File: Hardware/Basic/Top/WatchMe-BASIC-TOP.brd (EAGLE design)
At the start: 38 x 38 mm, 65 parts, among them SW1 SWITCH.MOM, SW2 SWITCH.MOM, U2 NRF52832_MODULE_MDBT42, U4 PCF8523, U5 FT231XS

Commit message: continuin top board work
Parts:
- removed C10, C11: 300p, LinnesLab-Passives:C0603
- removed R15: 100k, LinnesLab-Passives:R0603
- moved R19 49.2 mm to (12.4, 10.7), turned to 90 degrees
- moved R9 48.6 mm to (7.85, 15.5), turned to 0 degrees
- moved JP2 47.7 mm to (2.29, 7.72)
- moved LED5 47.6 mm to (13.9, 10.5), turned to 90 degrees
- moved C2 47.6 mm to (9.70, 2.11), turned to 0 degrees
- moved R20 46.7 mm to (3.20, 4.42)
- moved U5 46.4 mm to (7.24, 8.84)
- moved LED6 46.2 mm to (7.75, 3.58)
- moved C22 46.1 mm to (15.3, 9.09)
- moved R17 45.5 mm to (12.1, 7.34)
- moved R18 45.5 mm to (12.1, 4.19)
- moved C24 44.9 mm to (13.6, 7.39)
- moved D1 44.9 mm to (3.20, 24.4), turned to 180 degrees
- moved C23 44.9 mm to (13.6, 4.19)
- moved R8 44.7 mm to (11.5, 13.2), turned to 0 degrees
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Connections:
- net 3.3V: no longer R15.2
- net GND: no longer C10.2, C11.2, R15.1, SW1.B2, SW2.B2
- net P0.09/NFC1: no longer C11.1
- net P0.10/NFC2: no longer C10.1
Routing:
- net GND: track 0.00 -> 49.8 mm, vias 0 -> 20
- net D15/SW2: track 0.00 -> 35.7 mm
- net VLIPO: track 0.00 -> 13.8 mm
- net N$6: track 0.00 -> 10.9 mm
- net N$4: track 0.00 -> 10.8 mm
- net VIN: track 0.00 -> 10.4 mm
- net N$15: track 0.00 -> 10.4 mm
- net N$2: track 0.00 -> 10.1 mm
- net RESET: track 0.00 -> 9.97 mm
- net N$13: track 0.00 -> 9.50 mm
- net RXD.FT: track 0.00 -> 8.97 mm
- net SCL: track 0.00 -> 8.36 mm
- net V_USB: track 0.00 -> 7.84 mm
- net SDA: track 0.00 -> 7.11 mm
- net 3.3V: track 0.00 -> 4.59 mm, vias 0 -> 1
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- added copper zone on layer 1, net 9V
- added copper zone on layer 16, net GND

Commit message: updated top board, still pretty chaotic
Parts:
- moved SW3 27.6 mm to (14.1, 30.9), turned to 180 degrees
- moved LED4 26.1 mm to (14.5, 28.7), turned to 0 degrees
- moved LED3 26.0 mm to (14.4, 24.6), turned to 0 degrees
- moved R4 25.9 mm to (14.5, 27.4), turned to 0 degrees
- moved R3 25.9 mm to (14.5, 25.9), turned to 0 degrees
- moved C21 5.10 mm to (16.7, 11.3), turned to 180 degrees
- moved XTAL3 1.67 mm to (17.8, 22.8)
- moved SW2 1.15 mm to (22.3, 4.22)
- moved R14 1.04 mm to (18.1, 13.7)
- moved R13 0.97 mm to (16.5, 13.7)
- moved XTAL2 0.62 mm to (20.3, 22.4)
- moved L2 0.41 mm to (24.1, 25.1)
- moved J2 0.40 mm to (2.34, 16.3)
- moved C12 0.33 mm to (23.4, 22.6)
- moved CHRG2 0.23 mm to (8.92, 4.01)
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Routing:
- net RXD.NRF: track 0.00 -> 41.7 mm, vias 0 -> 2
- net MOSI: track 0.00 -> 40.1 mm, vias 0 -> 2
- net USB+: track 1.47 -> 40.1 mm, vias 0 -> 2
- net SWO: track 0.00 -> 36.8 mm, vias 0 -> 1
- net SCK: track 0.00 -> 35.4 mm, vias 0 -> 2
- net SWCLK: track 0.00 -> 34.6 mm, vias 0 -> 1
- net RESET: track 9.97 -> 44.2 mm, vias 0 -> 2
- net TXD.NRF: track 0.00 -> 32.8 mm, vias 0 -> 2
- net SWDIO: track 0.00 -> 32.4 mm, vias 0 -> 1
- net GND: track 49.8 -> 80.1 mm, vias 20 -> 23
- net D11/SW1: track 0.00 -> 29.9 mm, vias 0 -> 2
- net D27/CHRG.STATUS: track 3.97 -> 32.0 mm, vias 0 -> 1
- net USB-: track 1.52 -> 28.5 mm, vias 0 -> 1
- net D16/CS.OLED: track 0.00 -> 26.6 mm, vias 0 -> 2
- net D7/SD.CS: track 0.00 -> 26.1 mm, vias 0 -> 1
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
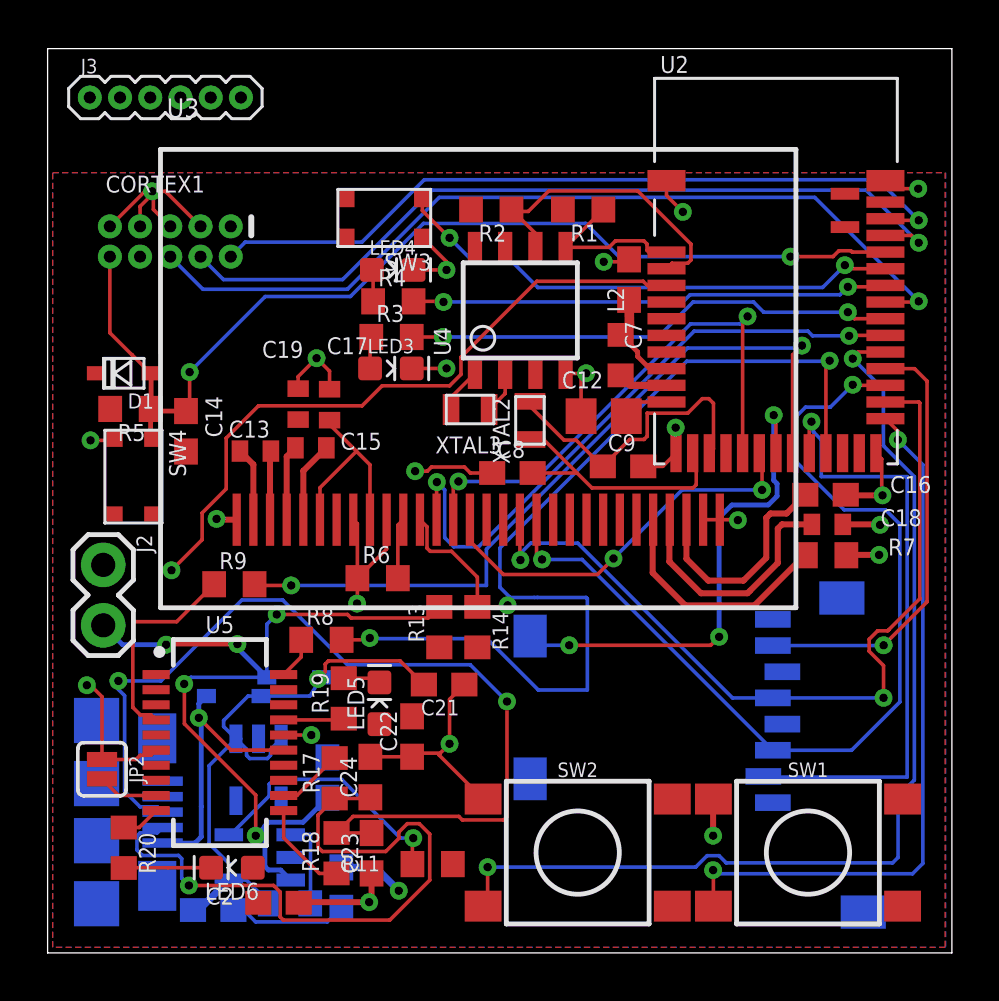
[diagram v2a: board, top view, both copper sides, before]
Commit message: top board routing complete
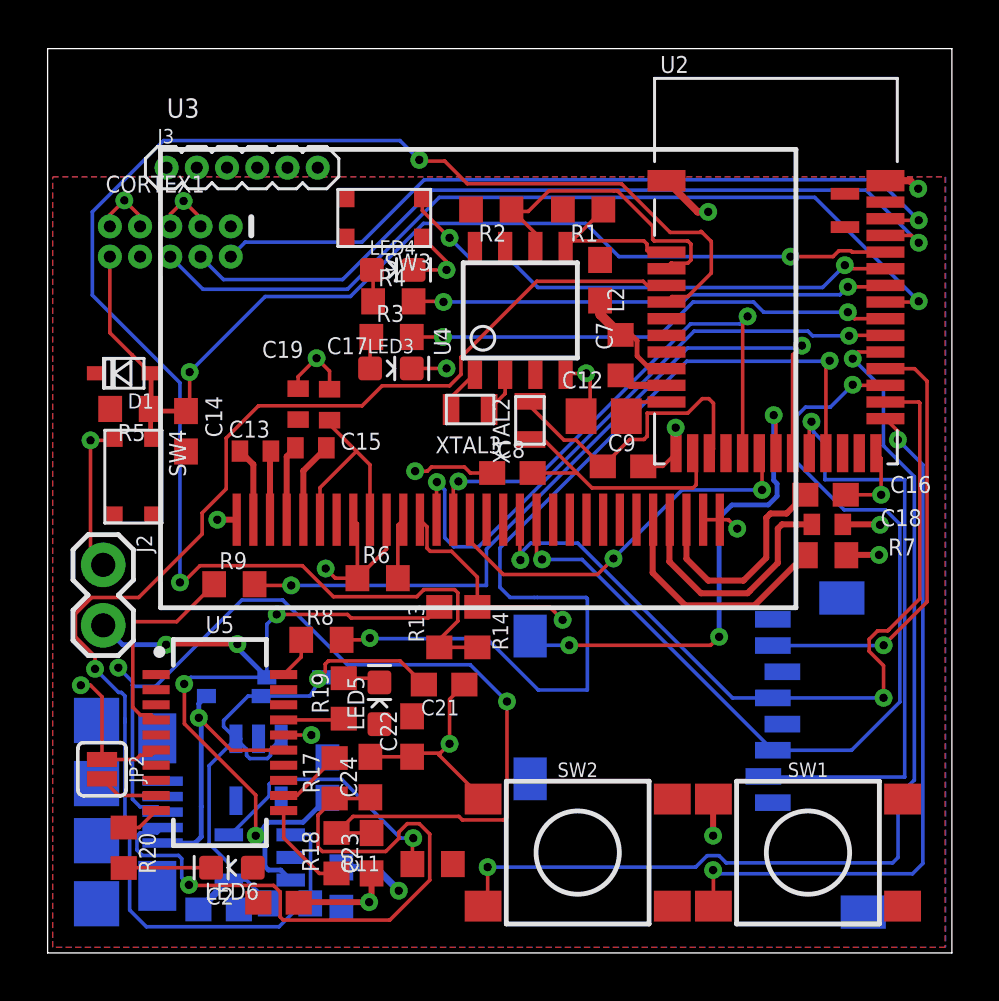
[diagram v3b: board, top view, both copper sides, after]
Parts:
- moved J3 4.37 mm to (5.00, 33.0)
- moved C7 1.22 mm to (23.2, 28.3)
- moved C5 0.23 mm to (7.19, 1.83)
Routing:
- net A4/BATT: track 0.00 -> 66.8 mm, vias 0 -> 2
- net D27/CHRG.STATUS: track 32.0 -> 58.5 mm
- net GND: track 80.1 -> 81.1 mm
- net SCL: track 13.2 -> 14.0 mm

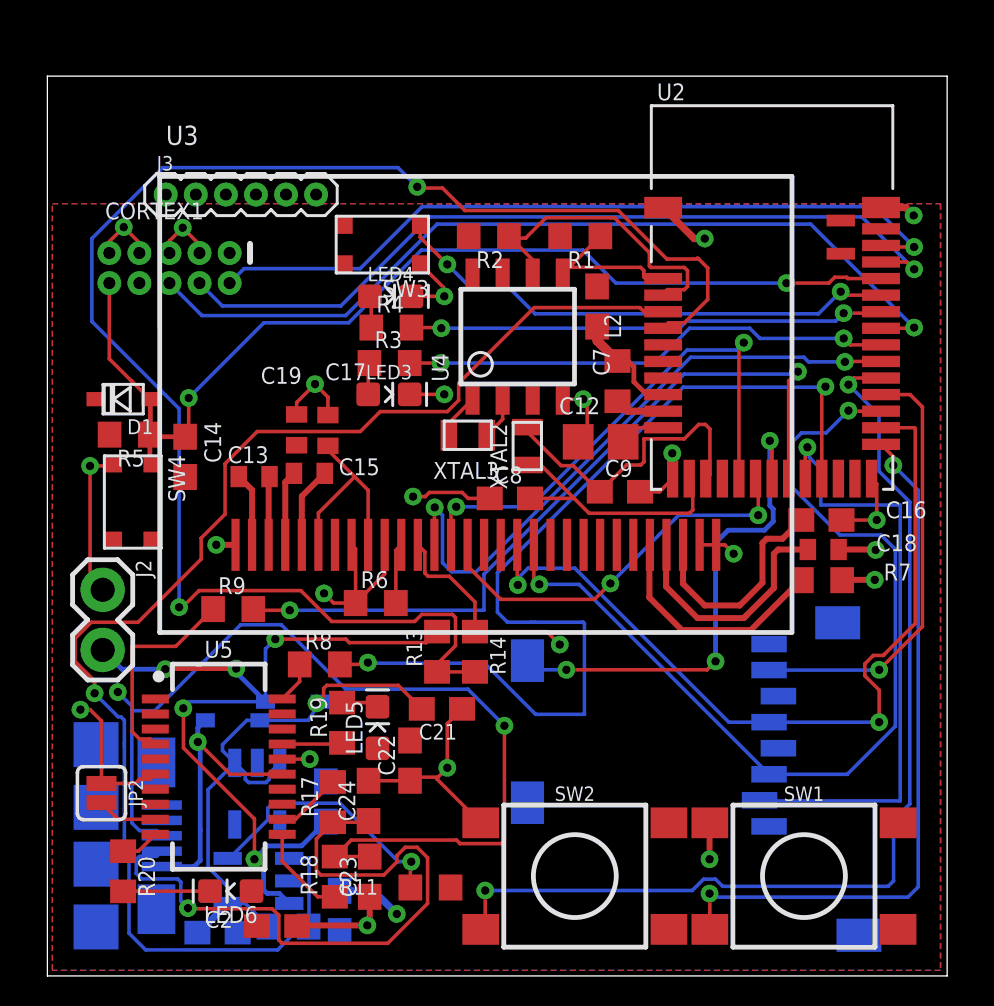
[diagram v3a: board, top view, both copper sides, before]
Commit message: Added LSM6DS3 sensor
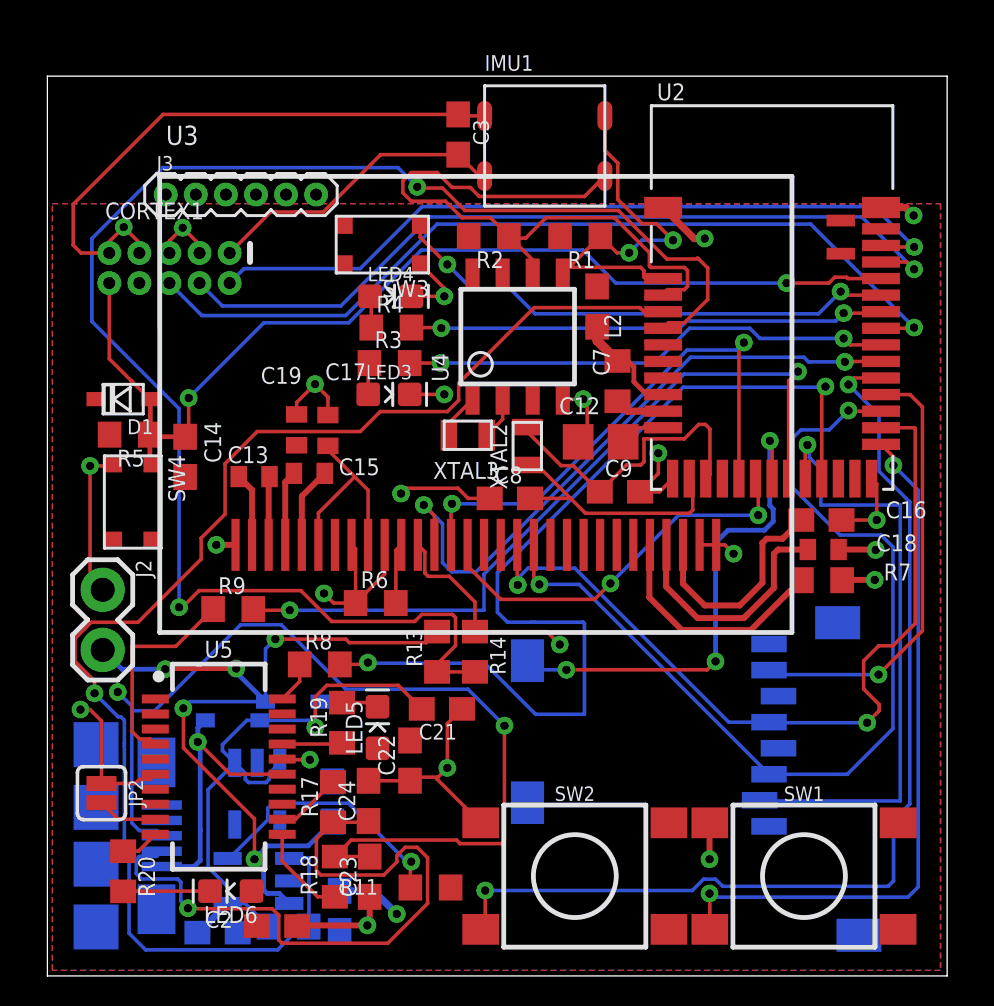
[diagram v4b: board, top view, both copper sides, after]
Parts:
- added C3: 100n, LinnesLab-Passives:C0603
- added IMU1: LSM6DS3_CAST, LinnesLab-Sensors:LSM6DS3_CAST
- moved C20 0.28 mm to (12.0, 7.37)
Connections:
- net 3.3V: now also C3.2, IMU1.2
- net GND: now also C3.1, IMU1.1
- net SCL: now also IMU1.3
- net SDA: now also IMU1.4
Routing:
- net GND: track 81.1 -> 104.9 mm
- net SCL: track 14.0 -> 29.2 mm
- net 3.3V: track 13.2 -> 26.0 mm
- net SDA: track 6.95 -> 17.3 mm, vias 0 -> 2
- net D16/CS.OLED: track 26.6 -> 27.1 mm
- net VIN: track 25.1 -> 25.6 mm

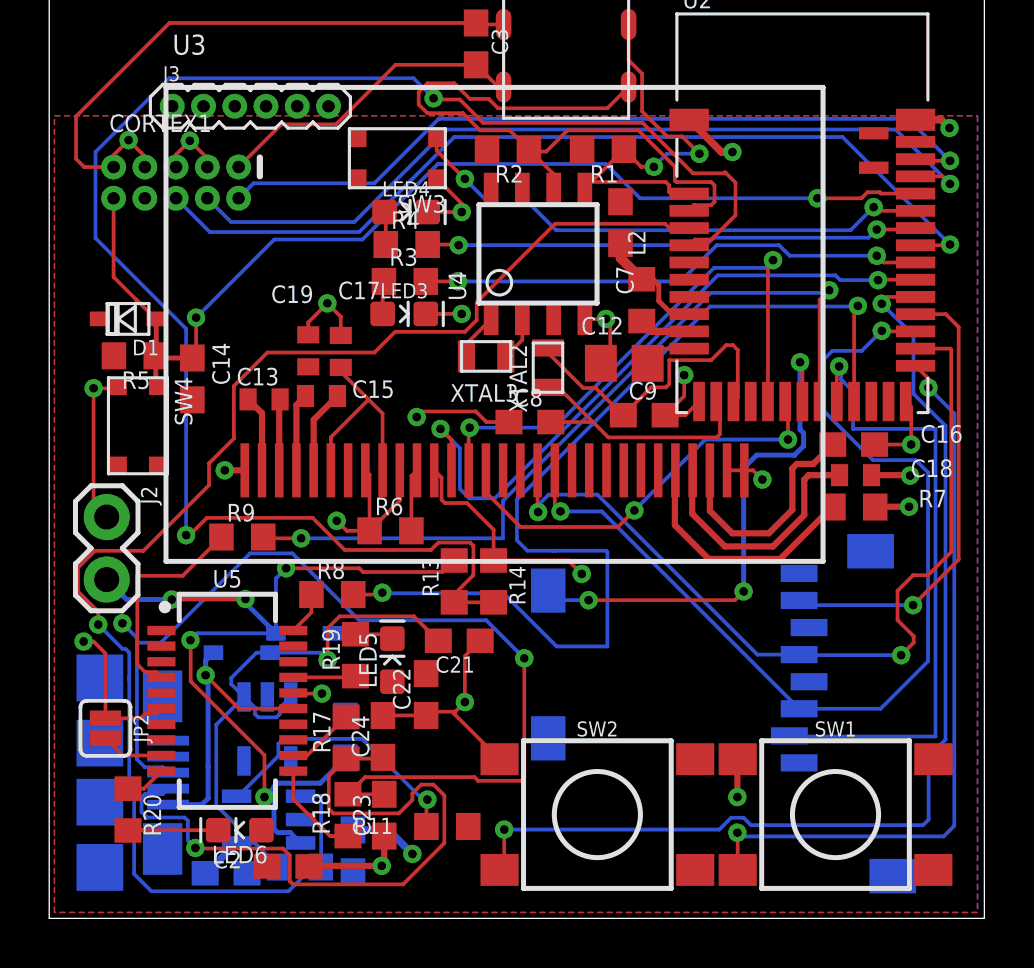
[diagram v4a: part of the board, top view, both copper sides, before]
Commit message: Beginning to resolve DRC errors
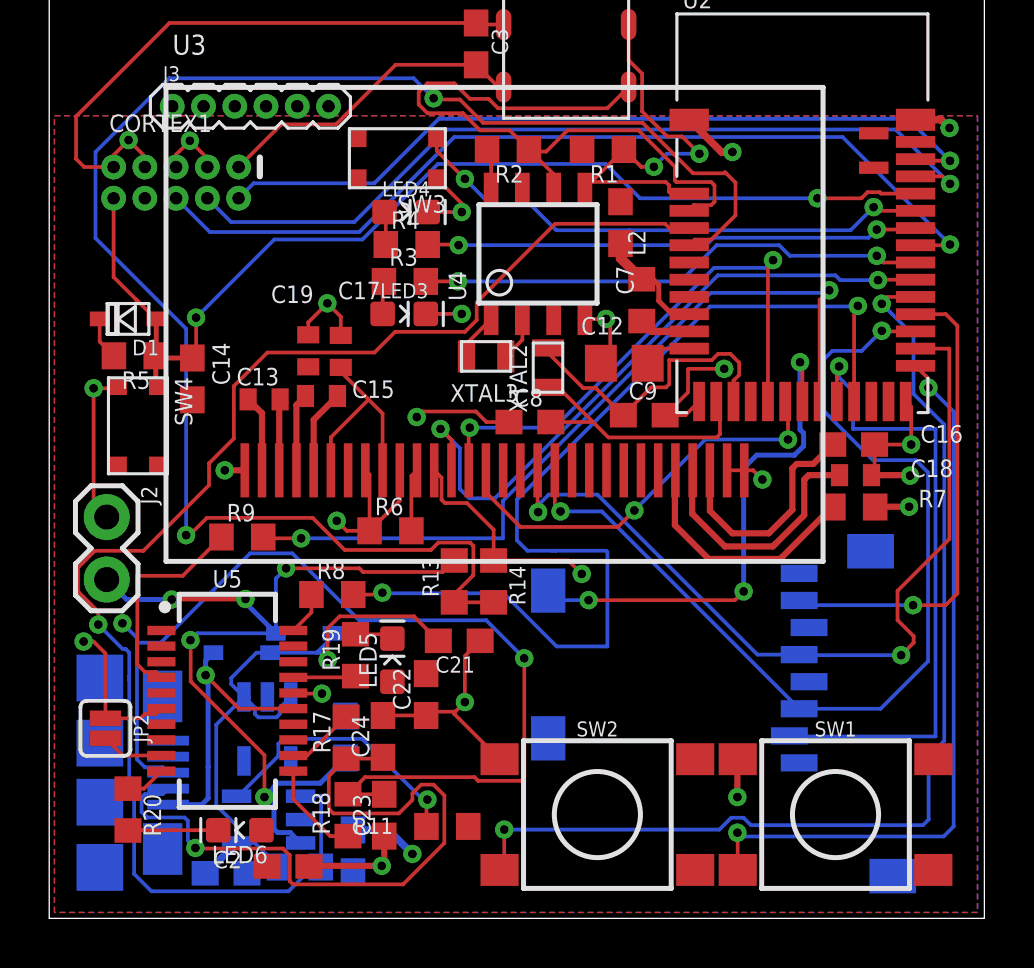
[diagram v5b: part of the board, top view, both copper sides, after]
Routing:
- net 3.3V: track 26.0 -> 29.4 mm
- net GND: track 104.9 -> 108.0 mm
- net VIN: track 25.6 -> 26.6 mm
- net MISO: track 18.7 -> 19.5 mm
- net N$6: track 13.0 -> 12.4 mm

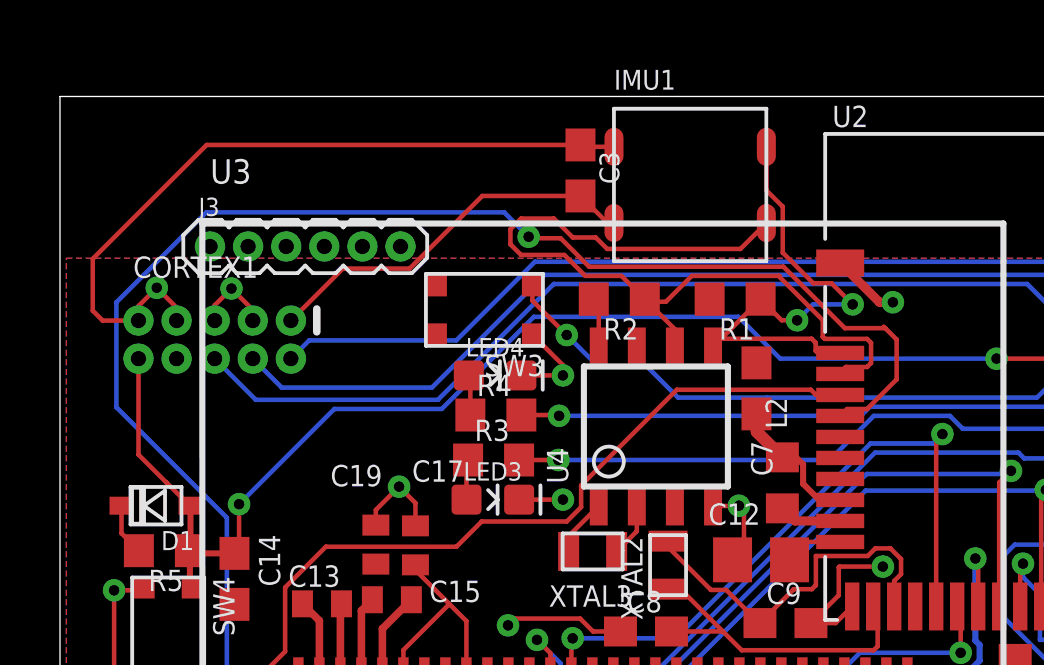
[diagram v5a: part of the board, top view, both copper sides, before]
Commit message: removed LSM6DS3 sensor - already on bottom board
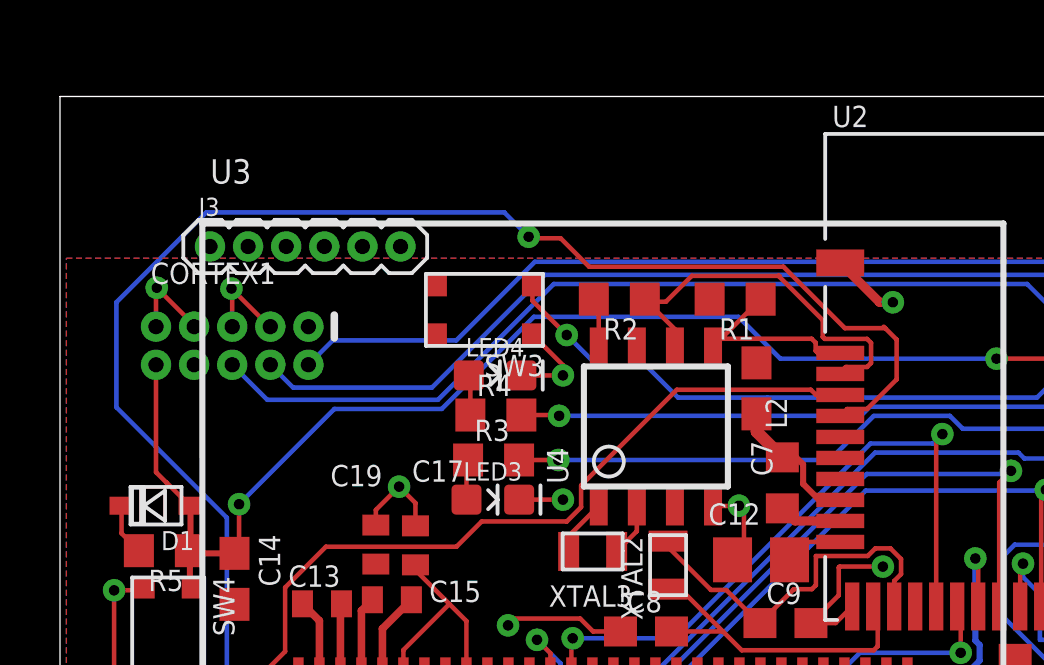
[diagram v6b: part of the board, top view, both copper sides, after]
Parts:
- removed C3: 100n, LinnesLab-Passives:C0603
- removed IMU1: LSM6DS3_CAST, LinnesLab-Sensors:LSM6DS3_CAST
- moved CORTEX1 0.62 mm to (5.74, 29.7)
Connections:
- net 3.3V: no longer C3.2, IMU1.2
- net GND: no longer C3.1, IMU1.1
- net SCL: no longer IMU1.3
- net SDA: no longer IMU1.4
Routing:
- net GND: track 108.0 -> 86.4 mm
- net SCL: track 29.2 -> 14.0 mm
- net 3.3V: track 29.4 -> 16.6 mm
- net SDA: track 17.3 -> 6.95 mm, vias 2 -> 0
- net SWO: track 36.8 -> 36.2 mm
- net SWCLK: track 34.6 -> 33.9 mm
- net SWDIO: track 32.4 -> 31.9 mm
